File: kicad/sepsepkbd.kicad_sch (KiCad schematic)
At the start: 20 parts, among them J1 Conn_01x10_Pin, J2 MJ-4PP-9, J3 Conn_01x08_Pin, J4 Conn_01x10_Pin, J5 MJ-4PP-9, J6 Conn_01x08_Pin, SW1 SW_PUSH, SW2 SW_PUSH, SW3 SW_PUSH, SW4 SW_PUSH, SW5 SW_PUSH, SW6 SW_PUSH, U1 RP2040-Zero, U2 RP2040-Zero

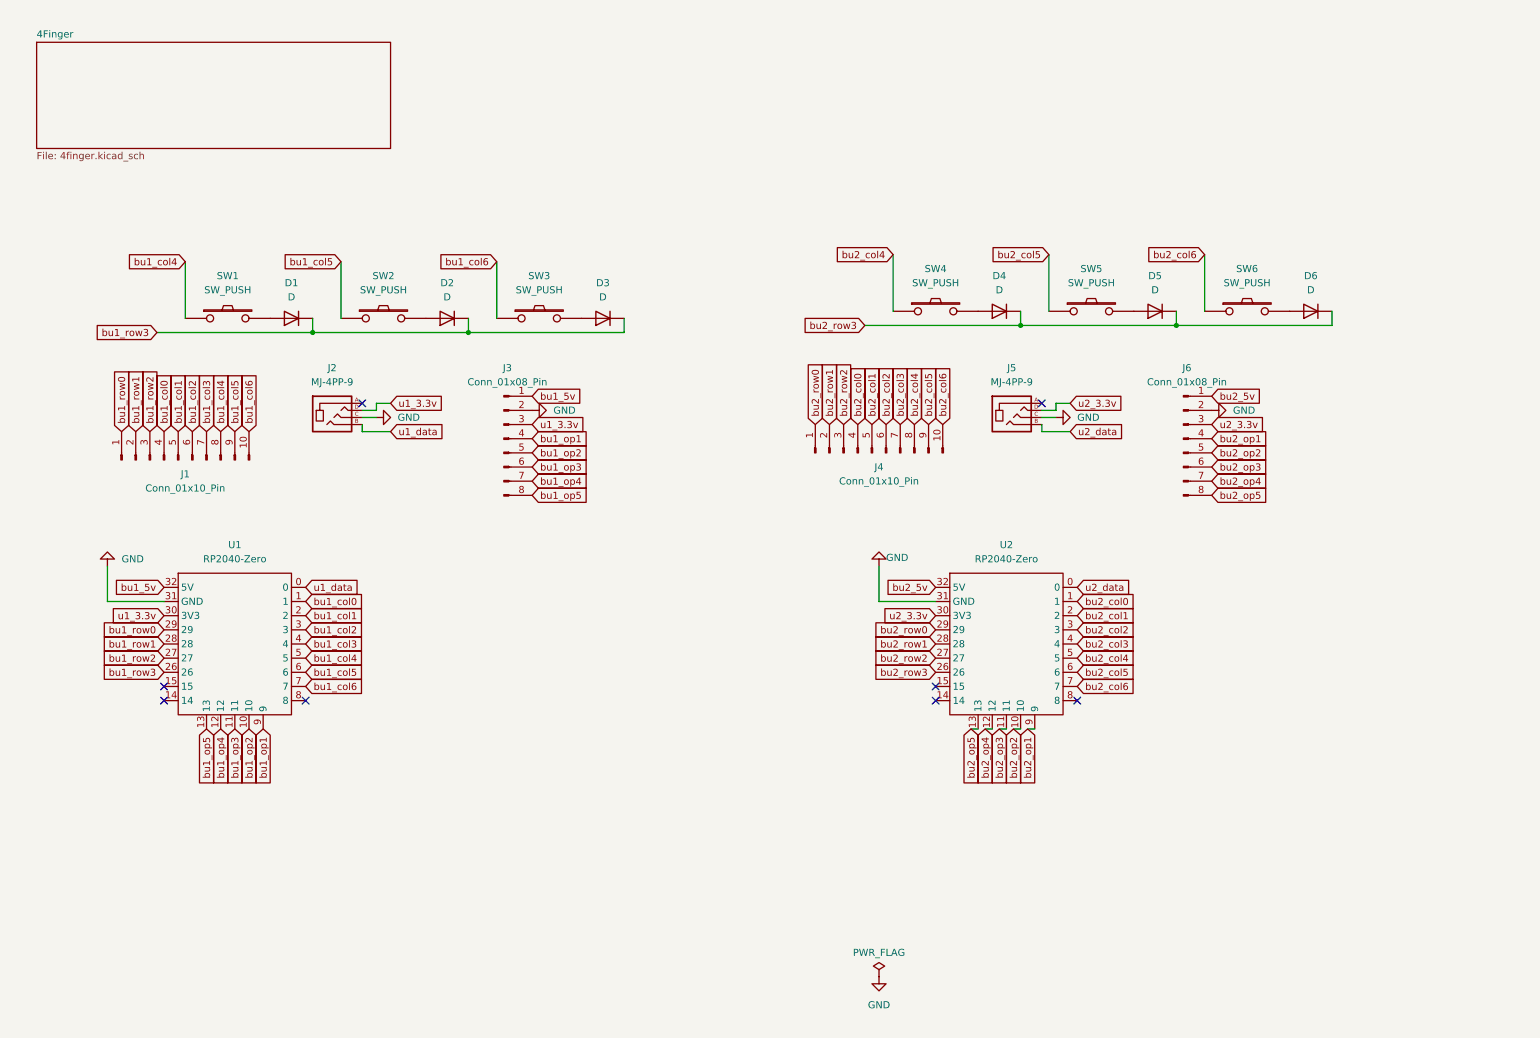
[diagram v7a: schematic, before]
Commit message: Add LEDs, and convert RP2040 to SMD
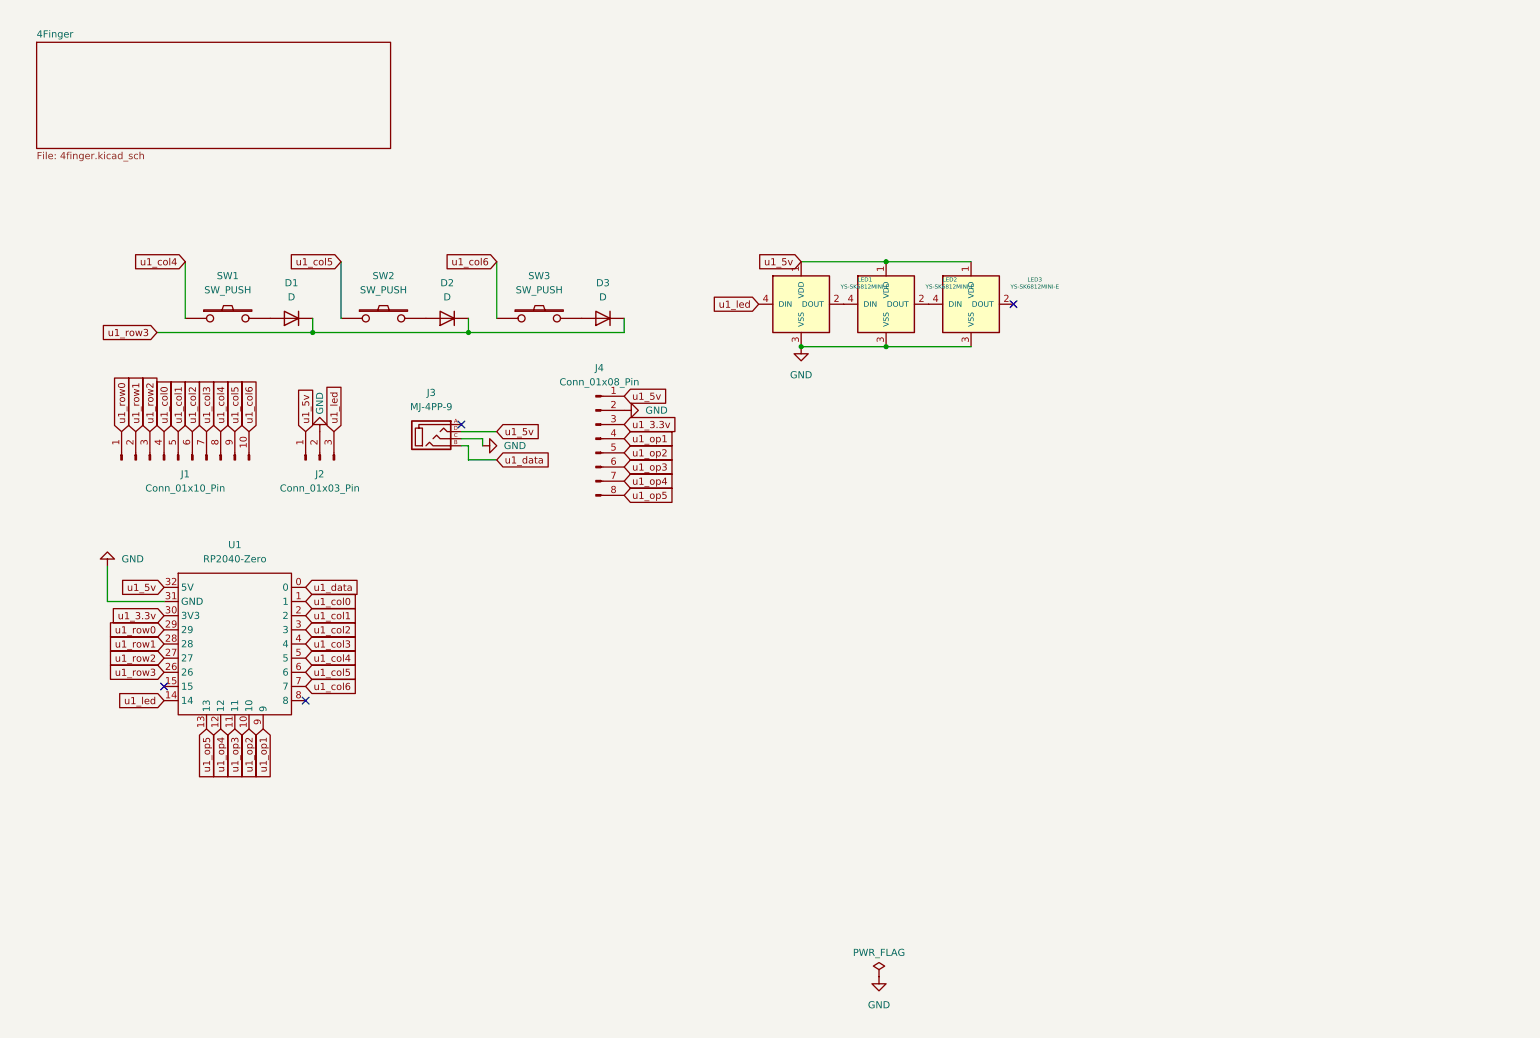
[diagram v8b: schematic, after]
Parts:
- removed D4, D5, D6: D, kbd:D3_SMD_v2, symbol Device:D
- removed J4: Conn_01x10_Pin, Connector_PinHeader_2.54mm:PinHeader_1x10_P2.54mm_Vertical, symbol Connector:Conn_01x10_Pin
- removed J5: MJ-4PP-9, kbd:MJ-4PP-9_1side, symbol kbd:MJ-4PP-9
- removed J6: Conn_01x08_Pin, Connector_PinHeader_2.54mm:PinHeader_1x08_P2.54mm_Vertical, symbol Connector:Conn_01x08_Pin
- removed SW4, SW5, SW6: SW_PUSH, keyswitches:Kailh_socket_PG1350, symbol kbd:SW_PUSH
- removed U2: RP2040-Zero, isw-kbd:RP2040-Zero-THT, symbol isw-mcu:RP2040-Zero
- added J2: Conn_01x03_Pin, Connector_PinHeader_2.54mm:PinHeader_1x03_P2.54mm_Vertical, symbol Connector:Conn_01x03_Pin
- added LED1, LED2, LED3: YS-SK6812MINI-E, sepsepkbd:YS-SK6812MINI-E, symbol kbd:YS-SK6812MINI-E
- D1, D2, D3: footprint kbd:D3_SMD_v2 -> kbd:D3_SMD
- J3: renamed from J2; footprint kbd:MJ-4PP-9_1side -> kbd:MJ-4PP-9
- SW1, SW2, SW3: footprint keyswitches:Kailh_socket_PG1350 -> keyswitches:Kailh_socket_PG1350_reversible
- U1: footprint isw-kbd:RP2040-Zero-THT -> sepsepkbd:WS-RP2040-Zero SMD
- renumbered J3 to J4
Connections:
- net GND: now also J2.2 (Pin_2), LED1.3 (VSS), LED2.3 (VSS), LED3.3 (VSS)
- net u1_3.3v: no longer J3.D
- net u1_led: now reaches U1.14
- net u1_led: now also J2.3 (Pin_3), LED1.4 (DIN)
- net bu1_5v renamed u1_5v
- net u1_5v: now also J3.D, J2.1 (Pin_1), LED1.1 (VDD), LED2.1 (VDD), LED3.1 (VDD)
- net bu1_col0 renamed u1_col0
- net bu1_col1 renamed u1_col1
- net bu1_col2 renamed u1_col2
- net bu1_col3 renamed u1_col3
- net bu1_col4 renamed u1_col4
- net bu1_col5 renamed u1_col5
- net bu1_col6 renamed u1_col6
- net bu1_op1 renamed u1_op1
- net bu1_op2 renamed u1_op2
- net bu1_op3 renamed u1_op3
- net bu1_op4 renamed u1_op4
- net bu1_op5 renamed u1_op5
- net bu1_row0 renamed u1_row0
- net bu1_row1 renamed u1_row1
- net bu1_row2 renamed u1_row2
- net bu1_row3 renamed u1_row3
- new net: LED1.2 (DOUT), LED2.4 (DIN)
- new net: LED2.2 (DOUT), LED3.4 (DIN)
- no-connect marks 8 -> 4
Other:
- moved on the sheet: J3, J4
